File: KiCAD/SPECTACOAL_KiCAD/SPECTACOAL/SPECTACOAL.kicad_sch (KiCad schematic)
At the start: 15 parts, among them SW1 Reset, SW2 Reset, U1 TiVa, U2 Joystick_2_Axis_1SW, U3 Joystick_2_Axis_1SW

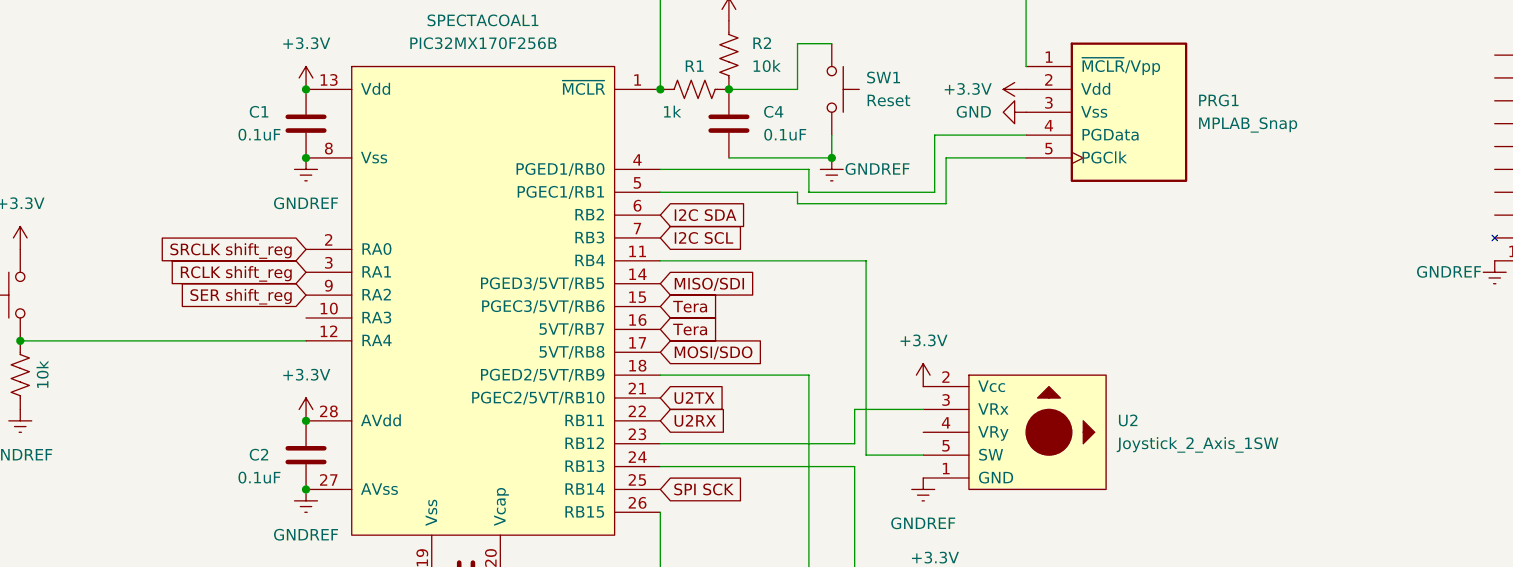
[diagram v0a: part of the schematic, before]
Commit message: add led indicator
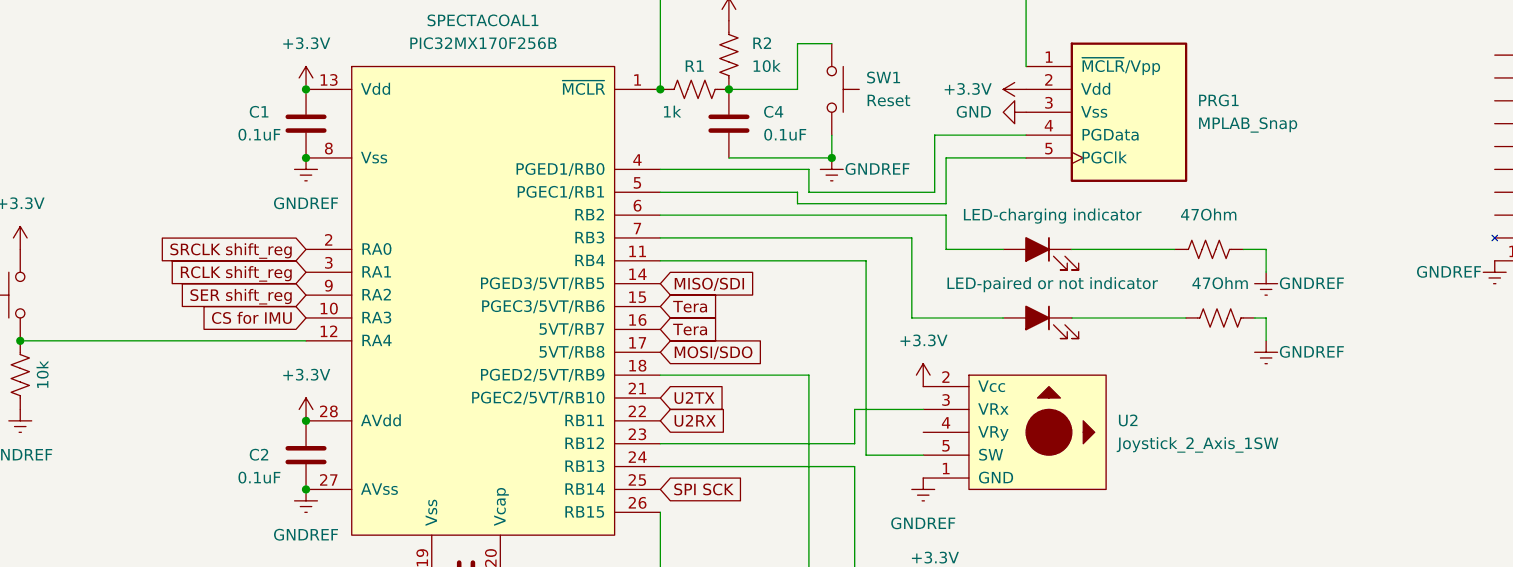
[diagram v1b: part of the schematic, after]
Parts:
- added D1: LED-charging indicator, symbol ME218_BaseLib:LED
- added D2: LED-paired or not indicator, symbol ME218_BaseLib:LED
- added R4, R5: 47Ohm, symbol ME218_BaseLib:Res1
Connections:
- net GNDREF: now also R4.2, R5.2
- net CS for IMU: now reaches SPECTACOAL1.10 (RA3)
- net I2C SCL: no longer names the net of SPECTACOAL1.7 (RB3)
- net I2C SCL: now also D2.2 (A)
- net I2C SDA: no longer names the net of SPECTACOAL1.6 (RB2)
- net I2C SDA: now also D1.2 (A)
- new net: D1.1 (K), R4.1
- new net: D2.1 (K), R5.1
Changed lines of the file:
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@@
+    (stroke (width 0) (type default))
+  )
+  (wire (pts (xy 166.37 74.93) (xy 153.67 74.93))
     (stroke (width 0) (type default))
   )
@@
     (stroke (width 0) (type default))
   )
+  (wire (pts (xy 139.7 67.31) (xy 139.7 63.5))
+    (stroke (width 0) (type default))
+  )
+  (wire (pts (xy 135.89 74.93) (xy 146.05 74.93))
+    (stroke (width 0) (type default))
+  )
+  (wire (pts (xy 146.05 67.31) (xy 139.7 67.31))
+    (stroke (width 0) (type default))
+  )
+  (wire (pts (xy 135.89 66.04) (xy 135.89 74.93))
+    (stroke (width 0) (type default))
+  )
   (wire (pts (xy 130.81 68.58) (xy 107.95 68.58))
     (stroke (width 0) (type default))
@@
     (stroke (width 0) (type default))
   )
+  (wire (pts (xy 175.26 67.31) (xy 172.72 67.31))
+    (stroke (width 0) (type default))
+  )
   (wire (pts (xy 107.95 91.44) (xy 129.54 91.44))
     (stroke (width 0) (type default))
@@
     (stroke (width 0) (type default))
   )
+  (wire (pts (xy 175.26 74.93) (xy 173.99 74.93))
+    (stroke (width 0) (type default))
+  )
   (wire (pts (xy 123.19 60.96) (xy 123.19 62.23))
     (stroke (width 0) (type default))
   )
+  (wire (pts (xy 139.7 63.5) (xy 107.95 63.5))
+    (stroke (width 0) (type default))
+  )
   (wire (pts (xy 123.19 44.45) (xy 127 44.45))
     (stroke (width 0) (type default))
@@
     (stroke (width 0) (type default))
   )
+  (wire (pts (xy 107.95 66.04) (xy 135.89 66.04))
+    (stroke (width 0) (type default))
+  )
   (wire (pts (xy 139.7 57.15) (xy 148.59 57.15))
     (stroke (width 0) (type default))
@@
     (stroke (width 0) (type default))
   )
+  (wire (pts (xy 175.26 67.31) (xy 175.26 69.85))
+    (stroke (width 0) (type default))
+  )
   (wire (pts (xy 123.19 62.23) (xy 139.7 62.23))
     (stroke (width 0) (type default))
@@
   )
   (wire (pts (xy 138.43 54.61) (xy 148.59 54.61))
+    (stroke (width 0) (type default))
+  )
+  (wire (pts (xy 165.1 67.31) (xy 153.67 67.31))
+    (stroke (width 0) (type default))
+  )
+  (wire (pts (xy 175.26 74.93) (xy 175.26 77.47))
     (stroke (width 0) (type default))
   )
@@
     )
   )
+  (global_label "CS for IMU" (shape input) (at 68.58 74.93 180) (fields_autoplaced)
+    (effects (font (size 1.27 1.27)) (justify right))
+    (property "Intersheetrefs" "${INTERSHEET_REFS}" (at 55.1325 74.93 0)
+      (effects (font (size 1.27 1.27)) (justify right) hide)
+    )
+  )
   (global_label "SER shift_reg" (shape input) (at 68.58 72.39 180) (fields_autoplaced)
     (effects (font (size 1.27 1.27)) (justify right))
@@
     )
   )
-  (global_label "I2C SCL" (shape input) (at 107.95 66.04 0) (fields_autoplaced)
-    (effects (font (size 1.27 1.27)) (justify left))
-    (property "Intersheetrefs" "${INTERSHEET_REFS}" (at 118.4947 66.04 0)
-      (effects (font (size 1.27 1.27)) (justify left) hide)
-    )
-  )
   (global_label "Tera" (shape input) (at 107.95 76.2 0) (fields_autoplaced)
     (effects (font (size 1.27 1.27)) (justify left))
@@
     (property "Intersheetrefs" "${INTERSHEET_REFS}" (at 50.3549 67.31 0)
       (effects (font (size 1.27 1.27)) (justify right) hide)
-    )
-  )
-  (global_label "I2C SDA" (shape input) (at 107.95 63.5 0) (fields_autoplaced)
-    (effects (font (size 1.27 1.27)) (justify left))
-    (property "Intersheetrefs" "${INTERSHEET_REFS}" (at 118.5552 63.5 0)
-      (effects (font (size 1.27 1.27)) (justify left) hide)
     )
   )
@@
     )
   )
+  (symbol (lib_id "ME218_BaseLib:LED") (at 149.86 67.31 0) (mirror y) (unit 1)
+    (in_bom yes) (on_board yes) (dnp no) (fields_autoplaced)
+    (property "Reference" "D1" (at 151.4602 60.96 0)
+      (effects (font (size 1.27 1.27)) hide)
+    )
+    (property "Value" "LED-charging indicator" (at 151.4602 63.5 0)
+      (effects (font (size 1.27 1.27)))
+    )
+    (property "Footprint" "" (at 149.86 67.31 0)
+      (effects (font (size 1.27 1.27)) hide)
+    )
+    (property "Datasheet" "" (at 149.86 67.31 0)
+      (effects (font (size 1.27 1.27)) hide)
+    )
+    (pin "1")
+    (pin "2")
+    (instances
+      (project "SPECTACOAL"
+        (path "/7b7f6bb2-7e9a-4004-b852-742946769482"
+          (reference "D1") (unit 1)
+        )
+      )
+    )
+  )
   (symbol (lib_id "power:+3.3V") (at 138.43 106.68 0) (unit 1)
     (in_bom yes) (on_board yes) (dnp no) (fields_autoplaced)
@@
     )
   )
+  (symbol (lib_id "ME218_BaseLib:Res1") (at 168.91 67.31 90) (unit 1)
+    (in_bom yes) (on_board yes) (dnp no) (fields_autoplaced)
+    (property "Reference" "R4" (at 168.91 60.96 90)
+      (effects (font (size 1.27 1.27)) hide)
+    )
+    (property "Value" "47Ohm" (at 168.91 63.5 90)
+      (effects (font (size 1.27 1.27)))
+    )
+    (property "Footprint" "" (at 169.164 66.294 90)
+      (effects (font (size 1.27 1.27)) hide)
+    )
+    (property "Datasheet" "" (at 168.91 67.31 0)
+      (effects (font (size 1.27 1.27)) hide)
+    )
+    (pin "1")
+    (pin "2")
+    (instances
+      (project "SPECTACOAL"
+        (path "/7b7f6bb2-7e9a-4004-b852-742946769482"
+          (reference "R4") (unit 1)
+        )
+      )
+    )
+  )
   (symbol (lib_id "ME218_BaseLib:Cap") (at 86.36 104.14 90) (unit 1)
     (in_bom yes) (on_board yes) (dnp no)
@@
     )
   )
+  (symbol (lib_id "power:GNDREF") (at 175.26 69.85 0) (unit 1)
+    (in_bom yes) (on_board yes) (dnp no)
+    (property "Reference" "#PWR020" (at 175.26 76.2 0)
+      (effects (font (size 1.27 1.27)) hide)
+    )
+    (property "Value" "GNDREF" (at 180.34 71.12 0)
+      (effects (font (size 1.27 1.27)))
+    )
+    (property "Footprint" "" (at 175.26 69.85 0)
+      (effects (font (size 1.27 1.27)) hide)
+    )
+    (property "Datasheet" "" (at 175.26 69.85 0)
+      (effects (font (size 1.27 1.27)) hide)
+    )
+    (pin "1")
+    (instances
+      (project "SPECTACOAL"
+        (path "/7b7f6bb2-7e9a-4004-b852-742946769482"
+          (reference "#PWR020") (unit 1)
+        )
+      )
+      (project "218CProjectKiCad"
+        (path "/90de9929-b4af-488b-8896-c9a198ebb96b"
+          (reference "#PWR034") (unit 1)
+        )
+      )
+    )
+  )
   (symbol (lib_id "power:GNDREF") (at 138.43 116.84 0) (unit 1)
     (in_bom yes) (on_board yes) (dnp no) (fields_autoplaced)
@@
     )
   )
+  (symbol (lib_id "ME218_BaseLib:Res1") (at 170.18 74.93 90) (unit 1)
+    (in_bom yes) (on_board yes) (dnp no) (fields_autoplaced)
+    (property "Reference" "R5" (at 170.18 68.58 90)
+      (effects (font (size 1.27 1.27)) hide)
+    )
+    (property "Value" "47Ohm" (at 170.18 71.12 90)
+      (effects (font (size 1.27 1.27)))
+    )
+    (property "Footprint" "" (at 170.434 73.914 90)
+      (effects (font (size 1.27 1.27)) hide)
+    )
+    (property "Datasheet" "" (at 170.18 74.93 0)
+      (effects (font (size 1.27 1.27)) hide)
+    )
+    (pin "1")
+    (pin "2")
+    (instances
+      (project "SPECTACOAL"
+        (path "/7b7f6bb2-7e9a-4004-b852-742946769482"
+          (reference "R5") (unit 1)
+        )
+      )
+    )
+  )
   (symbol (lib_id "power:+3.3V") (at 137.16 82.55 0) (unit 1)
     (in_bom yes) (on_board yes) (dnp no) (fields_autoplaced)
@@
         (path "/90de9929-b4af-488b-8896-c9a198ebb96b"
           (reference "C8") (unit 1)
+        )
+      )
+    )
+  )
+  (symbol (lib_id "ME218_BaseLib:LED") (at 149.86 74.93 0) (mirror y) (unit 1)
+    (in_bom yes) (on_board yes) (dnp no) (fields_autoplaced)
+    (property "Reference" "D2" (at 151.4602 68.58 0)
+      (effects (font (size 1.27 1.27)) hide)
+    )
+    (property "Value" "LED-paired or not indicator" (at 151.4602 71.12 0)
+      (effects (font (size 1.27 1.27)))
+    )
+    (property "Footprint" "" (at 149.86 74.93 0)
+      (effects (font (size 1.27 1.27)) hide)
+    )
+    (property "Datasheet" "" (at 149.86 74.93 0)
+      (effects (font (size 1.27 1.27)) hide)
+    )
+    (pin "1")
+    (pin "2")
+    (instances
+      (project "SPECTACOAL"
+        (path "/7b7f6bb2-7e9a-4004-b852-742946769482"
+          (reference "D2") (unit 1)
         )
       )
@@
         )
       )
+    )
+  )
+  (symbol (lib_id "power:GNDREF") (at 175.26 77.47 0) (unit 1)
+    (in_bom yes) (on_board yes) (dnp no)
+    (property "Reference" "#PWR019" (at 175.26 83.82 0)
+      (effects (font (size 1.27 1.27)) hide)
+    )
+    (property "Value" "GNDREF" (at 180.34 78.74 0)
+      (effects (font (size 1.27 1.27)))
+    )
+    (property "Footprint" "" (at 175.26 77.47 0)
+      (effects (font (size 1.27 1.27)) hide)
+    )
+    (property "Datasheet" "" (at 175.26 77.47 0)
+      (effects (font (size 1.27 1.27)) hide)
+    )
+    (pin "1")
+    (instances
+      (project "SPECTACOAL"
+        (path "/7b7f6bb2-7e9a-4004-b852-742946769482"
+          (reference "#PWR019") (unit 1)
+        )
+      )
+      (project "218CProjectKiCad"
+        (path "/90de9929-b4af-488b-8896-c9a198ebb96b"
+          (reference "#PWR034") (unit 1)
+        )
+      )

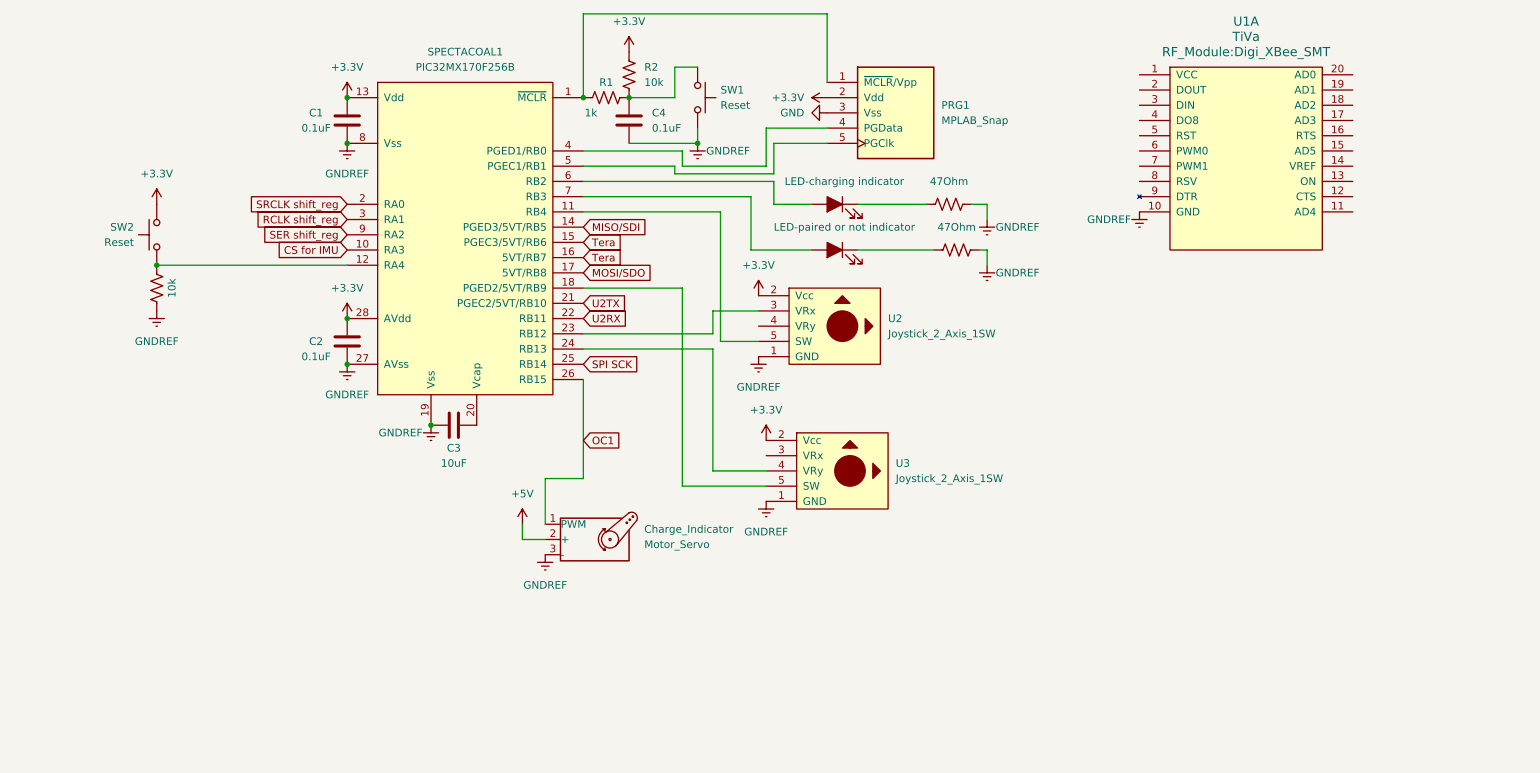
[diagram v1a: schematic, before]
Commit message: update kicad for 7 seg
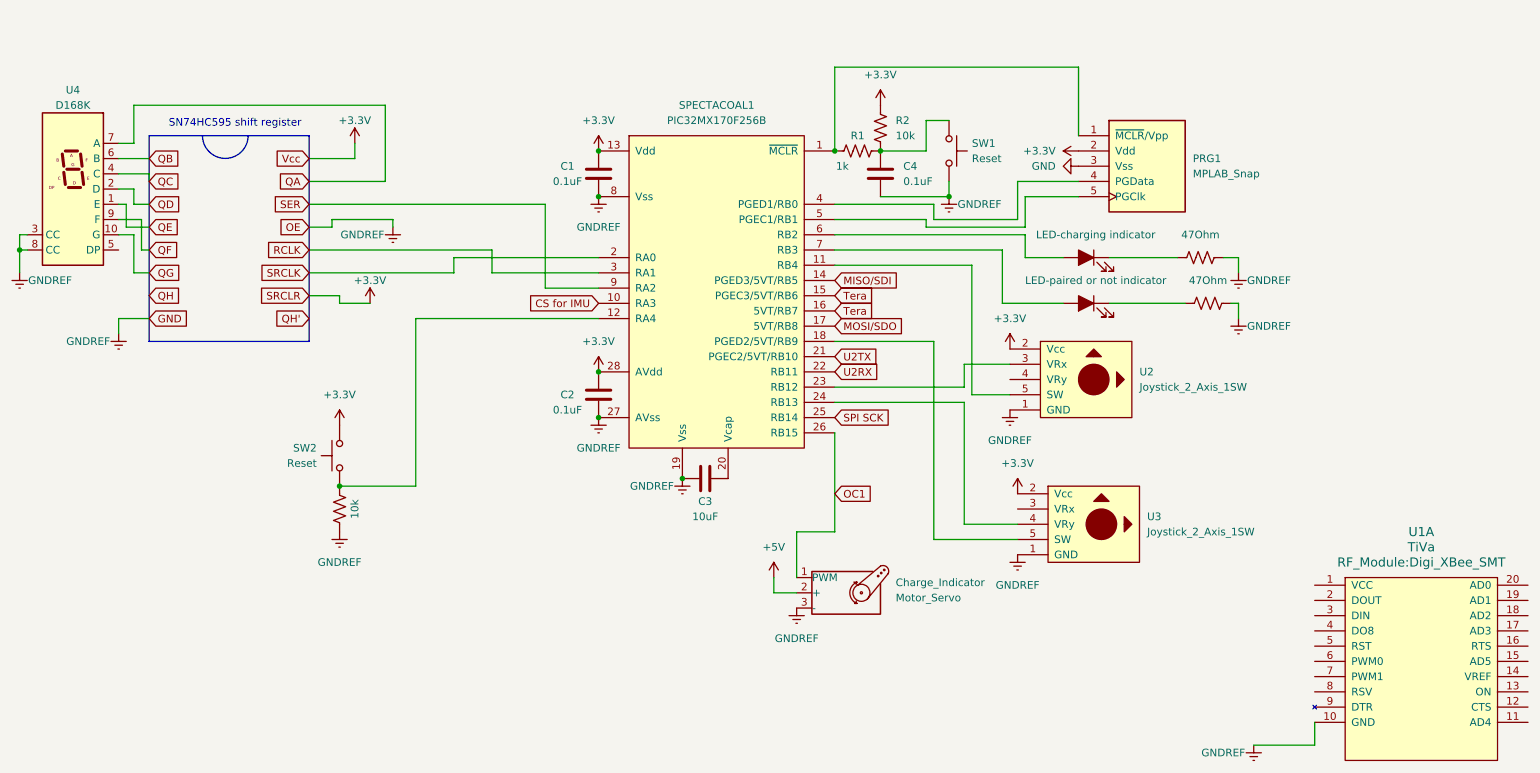
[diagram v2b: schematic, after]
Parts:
- added U4: D168K, Display_7Segment:D1X8K, symbol Display_Character:D168K
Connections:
- net GNDREF is gone; now on net GND: C1.2, C2.2, C3.1, C4.2, Charge_Indicator.3 (-), R3.1, R4.2, R5.2, SPECTACOAL1.19 (Vss), SPECTACOAL1.27 (AVss), SPECTACOAL1.8 (Vss), SW1.2, U1.10 (GND), U2.1 (GND), U3.1 (GND)
- net GND: now also U4.3 (CC), U4.8 (CC)
- net RCLK shift_reg renamed RCLK
- net SER shift_reg renamed SER
- net SRCLK shift_reg renamed SRCLK
- new net QA: U4.7 (A)
- new net QB: U4.6 (B)
- new net QC: U4.4 (C)
- new net QD: U4.2 (D)
- new net QE: U4.1 (E)
- new net QF: U4.9 (F)
- new net QG: U4.10 (G)
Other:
- note added: "SN74HC595 shift register"
- moved on the sheet: C1, C2, C3, C4, Charge_Indicator, PRG1, R1, R2, SPECTACOAL1, SW1, SW2, U1A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

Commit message: change buttons from idle low to idle high
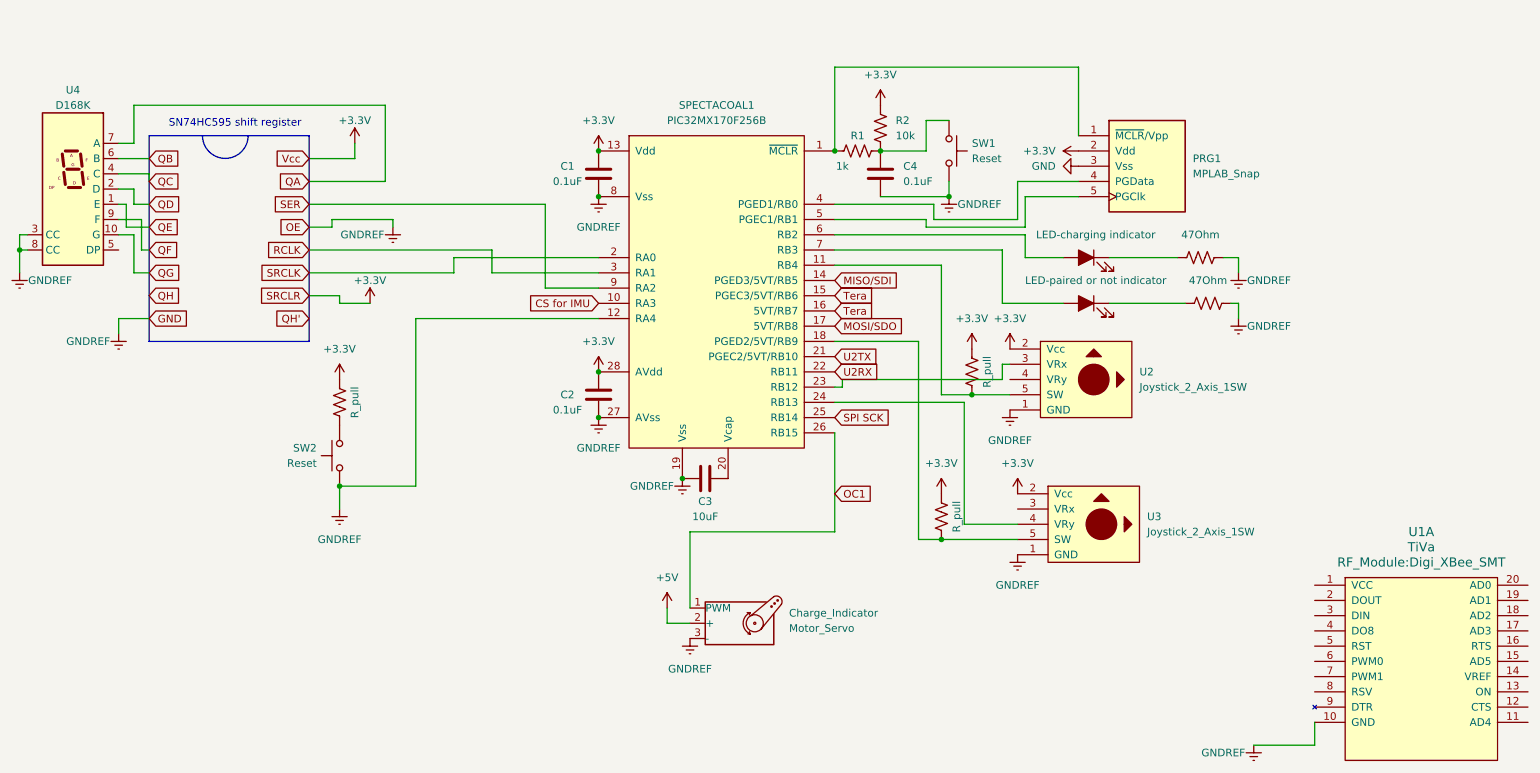
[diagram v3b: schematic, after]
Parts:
- added R6, R7: R_pull, symbol ME218_BaseLib:Res1
- R3: value 10k -> R_pull
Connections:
- net +3.3V: now also R3.2, R6.2, R7.2; no longer SW2.1
- net GND: now also SPECTACOAL1.12 (RA4), SW2.2; no longer R3.1
- net at SPECTACOAL1.11 (RB4), U2.5 (SW): now also R7.1
- net at SPECTACOAL1.18 (PGED2/5VT/RB9), U3.5 (SW): now also R6.1
- new net: R3.1, SW2.1
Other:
- moved on the sheet: Charge_Indicator
